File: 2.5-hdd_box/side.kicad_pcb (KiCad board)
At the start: 2 copper layers, 97 x 22.4 mm, 10 parts

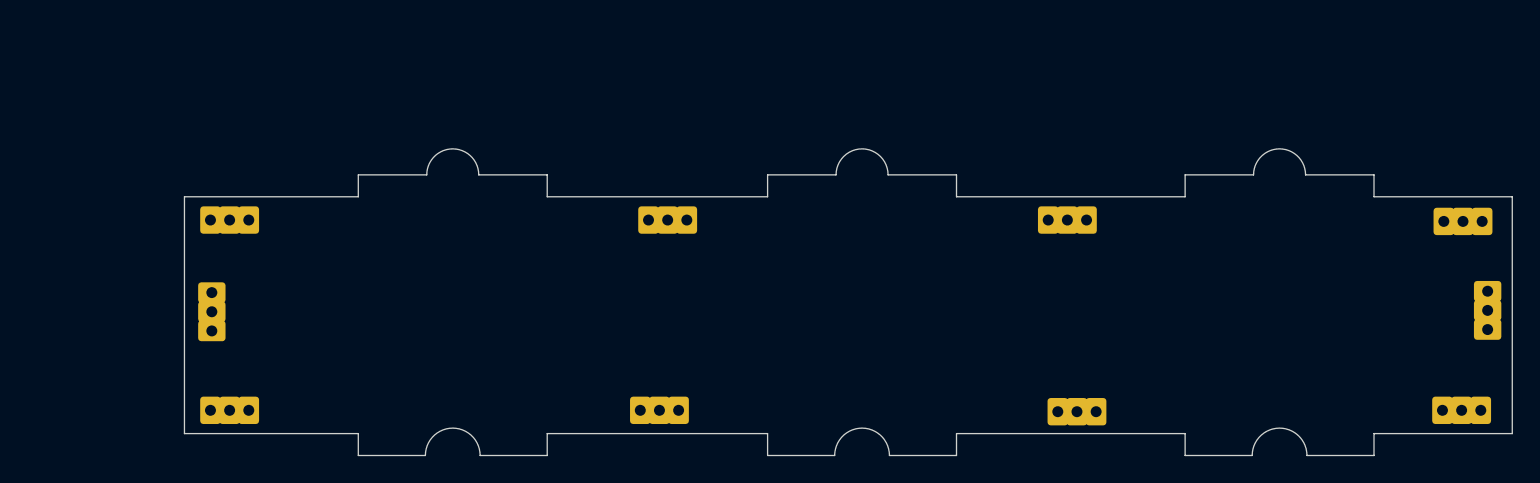
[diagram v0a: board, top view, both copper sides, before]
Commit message: 2.5-hdd_box: cut on bottom for usb-sata board, better placement of soldier pads
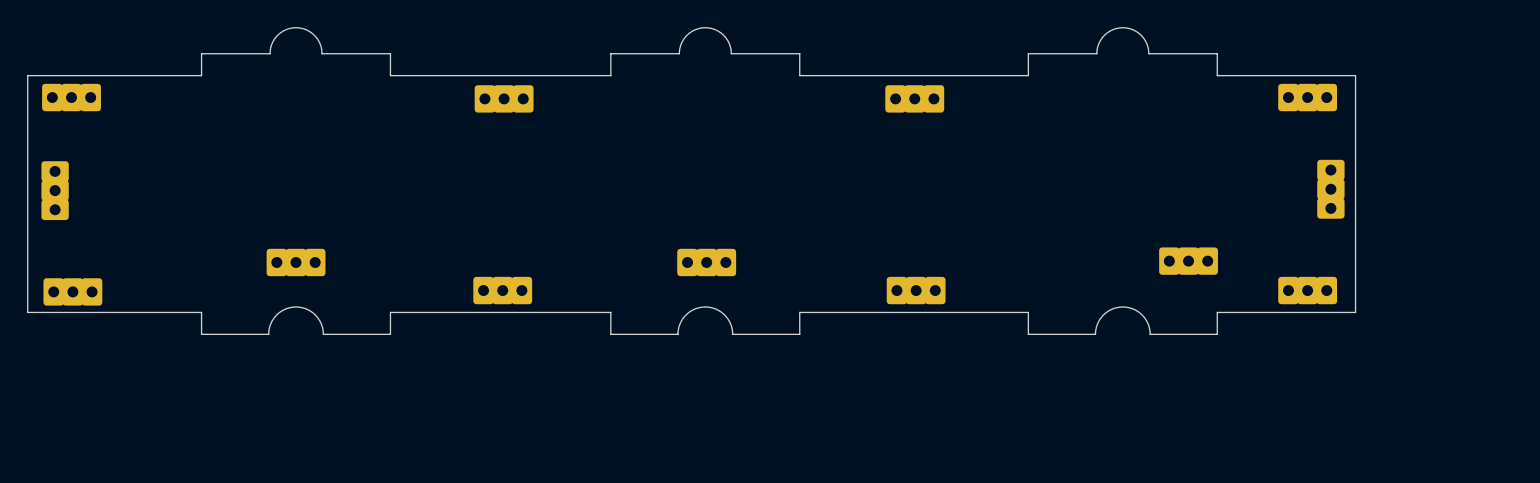
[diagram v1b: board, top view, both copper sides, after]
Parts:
- removed the REF** at (91.3, 78.9)
- removed the REF** at (58.5, 71.6)
- removed the REF** at (150.1, 65.1)
- removed the REF** at (149.9, 78.9)
- removed the REF** at (151.8, 71.5)
- removed the REF** at (121.2, 65.0)
- removed the REF** at (60.0, 65.0)
- removed the REF** at (121.8, 79.0)
- removed the REF** at (60.0, 78.9)
- removed the REF** at (92.0, 65.0)
- added REF**: soldpad, Local:soldpad, F.Cu at (138.7, 56.0)
- added REF**: soldpad, Local:soldpad, F.Cu at (94.8, 68.1)
- added REF**: soldpad, Local:soldpad, F.Cu at (64.8, 68.1)
- added REF**: soldpad, Local:soldpad, F.Cu at (80.0, 56.1)
- added REF**: soldpad, Local:soldpad, F.Cu at (130.0, 68.0)
- added REF**: soldpad, Local:soldpad, F.Cu at (140.3, 62.6)
- added REF**: soldpad, Local:soldpad, F.Cu at (47.1, 62.8)
- added REF**: soldpad, Local:soldpad, F.Cu at (110.1, 70.2)
- added REF**: soldpad, Local:soldpad, F.Cu at (110.0, 56.1)
- added REF**: soldpad, Local:soldpad, F.Cu at (79.9, 70.2)
- added REF**: soldpad, Local:soldpad, F.Cu at (138.7, 70.2)
- added REF**: soldpad, Local:soldpad, F.Cu at (48.5, 70.2)
- added REF**: soldpad, Local:soldpad, F.Cu at (48.4, 56.0)
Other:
- board text added: "Side"

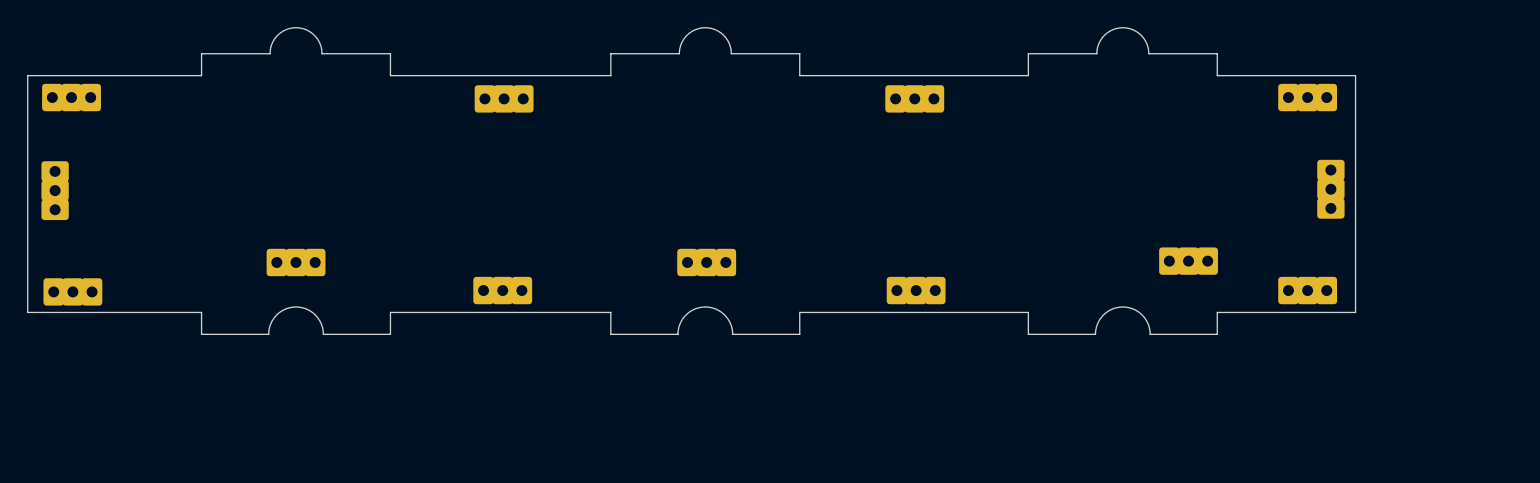
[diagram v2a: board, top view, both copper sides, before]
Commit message: height error on side corrected, cosmetics
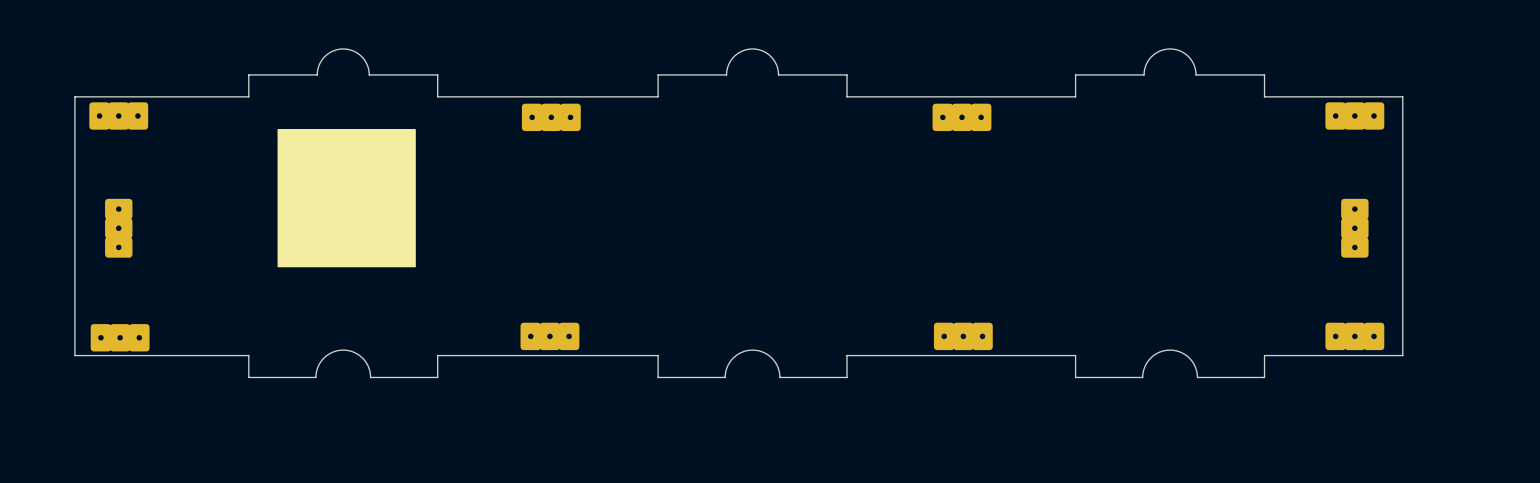
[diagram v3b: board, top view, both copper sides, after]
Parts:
- removed the REF** at (138.7, 56.0)
- removed the REF** at (94.8, 68.1)
- removed the REF** at (64.8, 68.1)
- removed the REF** at (80.0, 56.1)
- removed the REF** at (130.0, 68.0)
- removed the REF** at (140.3, 62.6)
- removed the REF** at (47.1, 62.8)
- removed the REF** at (110.1, 70.2)
- removed the REF** at (110.0, 56.1)
- removed the REF** at (79.9, 70.2)
- removed the REF** at (138.7, 70.2)
- removed the REF** at (48.5, 70.2)
- removed the REF** at (48.4, 56.0)
- added REF**: soldpad, Local:soldpad, F.Cu at (83.3, 73.5)
- added REF**: soldpad, Local:soldpad, F.Cu at (113.5, 57.5)
- added REF**: soldpad, Local:soldpad, F.Cu at (142.1, 65.5)
- added REF**: soldpad, Local:soldpad, F.Cu at (52.0, 73.6)
- added REF**: soldpad, Local:soldpad, F.Cu at (83.5, 57.5)
- added REF**: soldpad, Local:soldpad, F.Cu at (51.8, 65.5)
- added REF**: soldpad, Local:soldpad, F.Cu at (113.5, 73.5)
- added REF**: soldpad, Local:soldpad, F.Cu at (142.2, 57.4)
- added REF**: soldpad, Local:soldpad, F.Cu at (142.2, 73.5)
- added REF**: soldpad, Local:soldpad, F.Cu at (51.9, 57.4)
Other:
- board size 97 x 22.4 mm -> 97 x 24 mm

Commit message: last order has small mistakes, this one should be better. Other things added, your responsibility to discover
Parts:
- removed the REF** at (83.3, 73.5)
- removed the REF** at (113.5, 57.5)
- removed the REF** at (142.1, 65.5)
- removed the REF** at (52.0, 73.6)
- removed the REF** at (83.5, 57.5)
- removed the REF** at (51.8, 65.5)
- removed the REF** at (113.5, 73.5)
- removed the REF** at (142.2, 57.4)
- removed the REF** at (142.2, 73.5)
- removed the REF** at (51.9, 57.4)
- added REF**: soldpad, Local:soldpad, F.Cu at (142.0, 66.1)
- added REF**: soldpad, Local:soldpad, F.Cu at (142.2, 59.0)
- added REF**: soldpad, Local:soldpad, F.Cu at (52.1, 66.2)
- added REF**: soldpad, Local:soldpad, F.Cu at (97.1, 71.0)
- added REF**: soldpad, Local:soldpad, F.Cu at (65.8, 71.1)
- added REF**: soldpad, Local:soldpad, F.Cu at (128.6, 55.9)
- added REF**: soldpad, Local:soldpad, F.Cu at (81.0, 73.5)
- added REF**: soldpad, Local:soldpad, F.Cu at (142.2, 73.5)
- added REF**: soldpad, Local:soldpad, F.Cu at (65.6, 55.7)
- added REF**: soldpad, Local:soldpad, F.Cu at (52.0, 59.1)
- added REF**: soldpad, Local:soldpad, F.Cu at (128.7, 71.0)
- added REF**: soldpad, Local:soldpad, F.Cu at (52.0, 73.6)
- added REF**: soldpad, Local:soldpad, F.Cu at (97.1, 55.9)
- added REF**: soldpad, Local:soldpad, F.Cu at (113.6, 73.5)
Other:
- board size 97 x 24 mm -> 97 x 23.3 mm
